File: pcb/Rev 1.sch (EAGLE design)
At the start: 218 parts, among them J1 3220-10-0100-00, J2 10118194-0001LF, J3 B2B-PH-K-S(LF)(SN), Q1 MMBT3904,215MMBT3904,215, Q12 MMBT3904,215MMBT3904,215, Q13 MMBT3904,215MMBT3904,215, Q14 MMBT3904,215MMBT3904,215, Q15 MMBT3904,215MMBT3904,215, Q16 TEFT4300, Q17 TEFT4300, Q18 TEFT4300, Q19 TEFT4300, Q20 MMBT3904,215MMBT3904,215, Q21 MMBT3904,215MMBT3904,215, Q22 MMBT3904,215MMBT3904,215, Q23 MMBT3904,215MMBT3904,215, Q24 TEFT4300, Q25 TEFT4300, Q26 TEFT4300, Q27 TEFT4300, Q28 SI7157DP, Q29 SI7157DP, Q30 MMBT3906, Q31 MMBT3906, Q32 SI7157DP, Q33 MMBT3906, Q34 MMBT3906, U1 ATSAMD21G18A-MU, U10 DRV8871, U11 PCAL6416A, U12 MAX7315, U2 AP3441, U3 TPS61089, U4 BNO055, U5 MCP73811, U7 DRV8871, U8 DRV8871, U9 DRV8871

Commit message: Placed and routed IO expanders
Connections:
- net IR2: now also U11.P1_5; no longer U11.P1_1
- net IR3: now also U11.P1_4; no longer U11.P1_2
- net IR5: now also U11.P1_1; no longer U11.P1_4
- net IR6: now also U11.P1_2; no longer U11.P1_5
- net LED2: now also U11.P0_3; no longer U11.P0_2
- net LED3: now also U11.P0_4; no longer U11.P0_3
- net LED4: now also U11.P0_2; no longer U11.P0_4
- net MOTOR_1A: now also U12.P3; no longer U12.P1
- net MOTOR_1B: now also U12.P4; no longer U12.P2
- net MOTOR_2A: now also U12.P1; no longer U12.P3
- net MOTOR_2B: now also U12.P2; no longer U12.P4
- net MOTOR_3A: now also U12.P7; no longer U12.P5
- net MOTOR_3B: now also U12.P8; no longer U12.P6
- net MOTOR_4A: now also U12.P5; no longer U12.P7
- net MOTOR_4B: now also U12.P6; no longer U12.P8
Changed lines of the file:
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@@
 </segment>
 <segment>
-<pinref part="U12" gate="G$1" pin="P1"/>
-<wire x1="246.38" y1="0" x2="264.16" y2="0" width="0.1524" layer="91"/>
-<label x="248.92" y="0" size="1.778" layer="95"/>
+<pinref part="U12" gate="G$1" pin="P3"/>
+<wire x1="246.38" y1="-5.08" x2="264.16" y2="-5.08" width="0.1524" layer="91"/>
+<label x="248.92" y="-5.08" size="1.778" layer="95"/>
 </segment>
 </net>
@@
 </segment>
 <segment>
-<pinref part="U12" gate="G$1" pin="P2"/>
-<wire x1="264.16" y1="-2.54" x2="246.38" y2="-2.54" width="0.1524" layer="91"/>
-<label x="248.92" y="-2.54" size="1.778" layer="95"/>
+<pinref part="U12" gate="G$1" pin="P4"/>
+<wire x1="264.16" y1="-7.62" x2="246.38" y2="-7.62" width="0.1524" layer="91"/>
+<label x="248.92" y="-7.62" size="1.778" layer="95"/>
 </segment>
 </net>
@@
 </segment>
 <segment>
-<pinref part="U12" gate="G$1" pin="P3"/>
-<wire x1="246.38" y1="-5.08" x2="264.16" y2="-5.08" width="0.1524" layer="91"/>
-<label x="248.92" y="-5.08" size="1.778" layer="95"/>
+<pinref part="U12" gate="G$1" pin="P1"/>
+<wire x1="246.38" y1="0" x2="264.16" y2="0" width="0.1524" layer="91"/>
+<label x="248.92" y="0" size="1.778" layer="95"/>
 </segment>
 </net>
@@
 </segment>
 <segment>
-<pinref part="U12" gate="G$1" pin="P4"/>
-<wire x1="264.16" y1="-7.62" x2="246.38" y2="-7.62" width="0.1524" layer="91"/>
-<label x="248.92" y="-7.62" size="1.778" layer="95"/>
+<pinref part="U12" gate="G$1" pin="P2"/>
+<wire x1="264.16" y1="-2.54" x2="246.38" y2="-2.54" width="0.1524" layer="91"/>
+<label x="248.92" y="-2.54" size="1.778" layer="95"/>
 </segment>
 </net>
@@
 </segment>
 <segment>
+<pinref part="U12" gate="G$1" pin="P7"/>
+<wire x1="264.16" y1="-15.24" x2="246.38" y2="-15.24" width="0.1524" layer="91"/>
+<label x="248.92" y="-15.24" size="1.778" layer="95"/>
+</segment>
+</net>
+<net name="MOTOR_3B" class="0">
+<segment>
+<pinref part="U9" gate="G$1" pin="IN2"/>
+<wire x1="0" y1="-55.88" x2="-15.24" y2="-55.88" width="0.1524" layer="91"/>
+<label x="-15.24" y="-55.88" size="1.778" layer="95"/>
+</segment>
+<segment>
+<pinref part="U12" gate="G$1" pin="P8"/>
+<wire x1="264.16" y1="-17.78" x2="246.38" y2="-17.78" width="0.1524" layer="91"/>
+<label x="248.92" y="-17.78" size="1.778" layer="95"/>
+</segment>
+</net>
+<net name="ENCODER_3A" class="0">
+<segment>
+<pinref part="A3" gate="G$1" pin="OUTA"/>
+<wire x1="58.42" y1="-50.8" x2="38.1" y2="-50.8" width="0.1524" layer="91"/>
+<label x="38.1" y="-50.8" size="1.778" layer="95"/>
+</segment>
+</net>
+<net name="ENCODER_3B" class="0">
+<segment>
+<pinref part="A3" gate="G$1" pin="OUTB"/>
+<wire x1="58.42" y1="-53.34" x2="38.1" y2="-53.34" width="0.1524" layer="91"/>
+<label x="38.1" y="-53.34" size="1.778" layer="95"/>
+</segment>
+</net>
+<net name="MOTOR_4A" class="0">
+<segment>
+<pinref part="U10" gate="G$1" pin="IN1"/>
+<wire x1="106.68" y1="-53.34" x2="91.44" y2="-53.34" width="0.1524" layer="91"/>
+<label x="91.44" y="-53.34" size="1.778" layer="95"/>
+</segment>
+<segment>
 <pinref part="U12" gate="G$1" pin="P5"/>
 <wire x1="264.16" y1="-10.16" x2="246.38" y2="-10.16" width="0.1524" layer="91"/>
@@
 </segment>
 </net>
-<net name="MOTOR_3B" class="0">
-<segment>
-<pinref part="U9" gate="G$1" pin="IN2"/>
-<wire x1="0" y1="-55.88" x2="-15.24" y2="-55.88" width="0.1524" layer="91"/>
-<label x="-15.24" y="-55.88" size="1.778" layer="95"/>
+<net name="MOTOR_4B" class="0">
+<segment>
+<pinref part="U10" gate="G$1" pin="IN2"/>
+<wire x1="106.68" y1="-55.88" x2="91.44" y2="-55.88" width="0.1524" layer="91"/>
+<label x="91.44" y="-55.88" size="1.778" layer="95"/>
 </segment>
 <segment>
@@
 <wire x1="264.16" y1="-12.7" x2="246.38" y2="-12.7" width="0.1524" layer="91"/>
 <label x="248.92" y="-12.7" size="1.778" layer="95"/>
-</segment>
-</net>
-<net name="ENCODER_3A" class="0">
-<segment>
-<pinref part="A3" gate="G$1" pin="OUTA"/>
-<wire x1="58.42" y1="-50.8" x2="38.1" y2="-50.8" width="0.1524" layer="91"/>
-<label x="38.1" y="-50.8" size="1.778" layer="95"/>
-</segment>
-</net>
-<net name="ENCODER_3B" class="0">
-<segment>
-<pinref part="A3" gate="G$1" pin="OUTB"/>
-<wire x1="58.42" y1="-53.34" x2="38.1" y2="-53.34" width="0.1524" layer="91"/>
-<label x="38.1" y="-53.34" size="1.778" layer="95"/>
-</segment>
-</net>
-<net name="MOTOR_4A" class="0">
-<segment>
-<pinref part="U10" gate="G$1" pin="IN1"/>
-<wire x1="106.68" y1="-53.34" x2="91.44" y2="-53.34" width="0.1524" layer="91"/>
-<label x="91.44" y="-53.34" size="1.778" layer="95"/>
-</segment>
-<segment>
-<pinref part="U12" gate="G$1" pin="P7"/>
-<wire x1="264.16" y1="-15.24" x2="246.38" y2="-15.24" width="0.1524" layer="91"/>
-<label x="248.92" y="-15.24" size="1.778" layer="95"/>
-</segment>
-</net>
-<net name="MOTOR_4B" class="0">
-<segment>
-<pinref part="U10" gate="G$1" pin="IN2"/>
-<wire x1="106.68" y1="-55.88" x2="91.44" y2="-55.88" width="0.1524" layer="91"/>
-<label x="91.44" y="-55.88" size="1.778" layer="95"/>
-</segment>
-<segment>
-<pinref part="U12" gate="G$1" pin="P8"/>
-<wire x1="264.16" y1="-17.78" x2="246.38" y2="-17.78" width="0.1524" layer="91"/>
-<label x="248.92" y="-17.78" size="1.778" layer="95"/>
 </segment>
 </net>
@@
 <net name="LED2" class="0">
 <segment>
-<pinref part="U11" gate="G$1" pin="P0_2"/>
-<wire x1="0" y1="-45.72" x2="10.16" y2="-45.72" width="0.1524" layer="91"/>
-<label x="0" y="-45.72" size="1.778" layer="95"/>
-</segment>
-<segment>
 <pinref part="R18" gate="G$1" pin="P$1"/>
 <wire x1="63.5" y1="5.08" x2="63.5" y2="2.54" width="0.1524" layer="91"/>
@@
 <label x="55.88" y="2.54" size="1.778" layer="95"/>
 </segment>
-</net>
-<net name="LED3" class="0">
 <segment>
 <pinref part="U11" gate="G$1" pin="P0_3"/>
@@
 <label x="0" y="-48.26" size="1.778" layer="95"/>
 </segment>
+</net>
+<net name="LED3" class="0">
 <segment>
 <pinref part="R19" gate="G$1" pin="P$1"/>
@@
 <label x="78.74" y="2.54" size="1.778" layer="95"/>
 </segment>
-</net>
-<net name="LED4" class="0">
 <segment>
 <pinref part="U11" gate="G$1" pin="P0_4"/>
@@
 <label x="0" y="-50.8" size="1.778" layer="95"/>
 </segment>
+</net>
+<net name="LED4" class="0">
 <segment>
 <pinref part="R20" gate="G$1" pin="P$1"/>
@@
 <label x="101.6" y="2.54" size="1.778" layer="95"/>
 </segment>
+<segment>
+<pinref part="U11" gate="G$1" pin="P0_2"/>
+<wire x1="0" y1="-45.72" x2="10.16" y2="-45.72" width="0.1524" layer="91"/>
+<label x="0" y="-45.72" size="1.778" layer="95"/>
+</segment>
 </net>
 <net name="N$25" class="0">
@@
 </segment>
 </net>
-<net name="IR2" class="0">
+<net name="IR3" class="0">
+<segment>
+<pinref part="U11" gate="G$1" pin="P1_4"/>
+<wire x1="48.26" y1="-50.8" x2="40.64" y2="-50.8" width="0.1524" layer="91"/>
+<label x="43.18" y="-50.8" size="1.778" layer="95"/>
+</segment>
+</net>
+<net name="IR4" class="0">
+<segment>
+<pinref part="U11" gate="G$1" pin="P1_3"/>
+<wire x1="48.26" y1="-48.26" x2="40.64" y2="-48.26" width="0.1524" layer="91"/>
+<label x="43.18" y="-48.26" size="1.778" layer="95"/>
+</segment>
+</net>
+<net name="IR7" class="0">
+<segment>
+<pinref part="U11" gate="G$1" pin="P1_6"/>
+<wire x1="48.26" y1="-55.88" x2="40.64" y2="-55.88" width="0.1524" layer="91"/>
+<label x="43.18" y="-55.88" size="1.778" layer="95"/>
+</segment>
+</net>
+<net name="IR8" class="0">
+<segment>
+<pinref part="U11" gate="G$1" pin="P1_7"/>
+<wire x1="48.26" y1="-58.42" x2="40.64" y2="-58.42" width="0.1524" layer="91"/>
+<label x="43.18" y="-58.42" size="1.778" layer="95"/>
+</segment>
+</net>
+<net name="IR5" class="0">
 <segment>
 <pinref part="U11" gate="G$1" pin="P1_1"/>
@@
 </segment>
 </net>
-<net name="IR3" class="0">
+<net name="IR6" class="0">
 <segment>
 <pinref part="U11" gate="G$1" pin="P1_2"/>
@@
 </segment>
 </net>
-<net name="IR4" class="0">
-<segment>
-<pinref part="U11" gate="G$1" pin="P1_3"/>
-<wire x1="48.26" y1="-48.26" x2="40.64" y2="-48.26" width="0.1524" layer="91"/>
-<label x="43.18" y="-48.26" size="1.778" layer="95"/>
-</segment>
-</net>
-<net name="IR5" class="0">
-<segment>
-<pinref part="U11" gate="G$1" pin="P1_4"/>
-<wire x1="48.26" y1="-50.8" x2="40.64" y2="-50.8" width="0.1524" layer="91"/>
-<label x="43.18" y="-50.8" size="1.778" layer="95"/>
-</segment>
-</net>
-<net name="IR6" class="0">
+<net name="IR2" class="0">
 <segment>
 <pinref part="U11" gate="G$1" pin="P1_5"/>
@@
 </segment>
 </net>
-<net name="IR7" class="0">
-<segment>
-<pinref part="U11" gate="G$1" pin="P1_6"/>
-<wire x1="48.26" y1="-55.88" x2="40.64" y2="-55.88" width="0.1524" layer="91"/>
-<label x="43.18" y="-55.88" size="1.778" layer="95"/>
-</segment>
-</net>
-<net name="IR8" class="0">
-<segment>
-<pinref part="U11" gate="G$1" pin="P1_7"/>
-<wire x1="48.26" y1="-58.42" x2="40.64" y2="-58.42" width="0.1524" layer="91"/>
-<label x="43.18" y="-58.42" size="1.778" layer="95"/>
-</segment>
-</net>

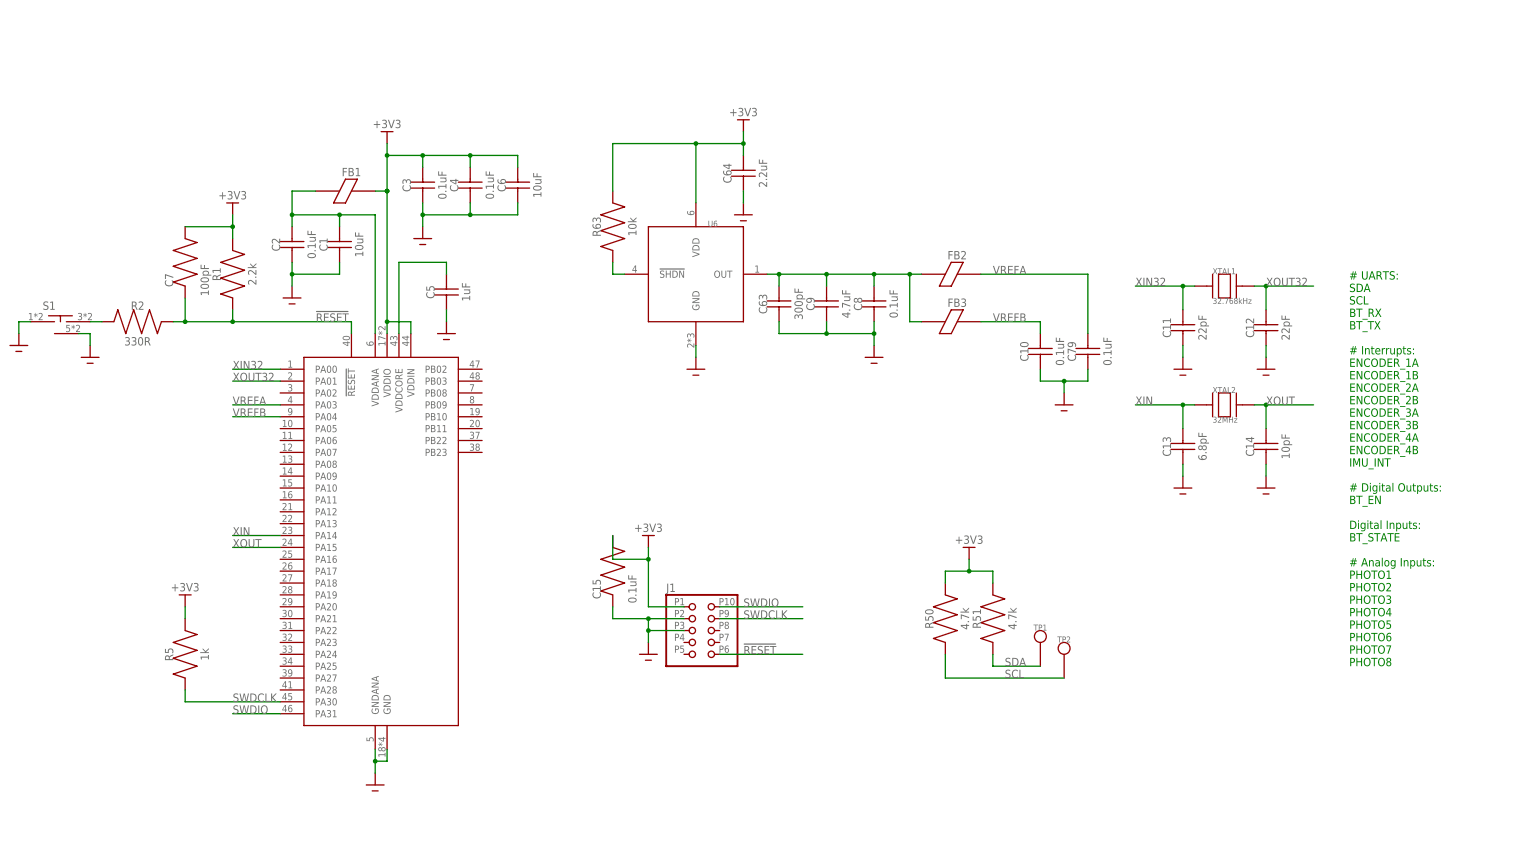
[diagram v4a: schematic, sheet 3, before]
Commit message: Finished routing signals to MCU
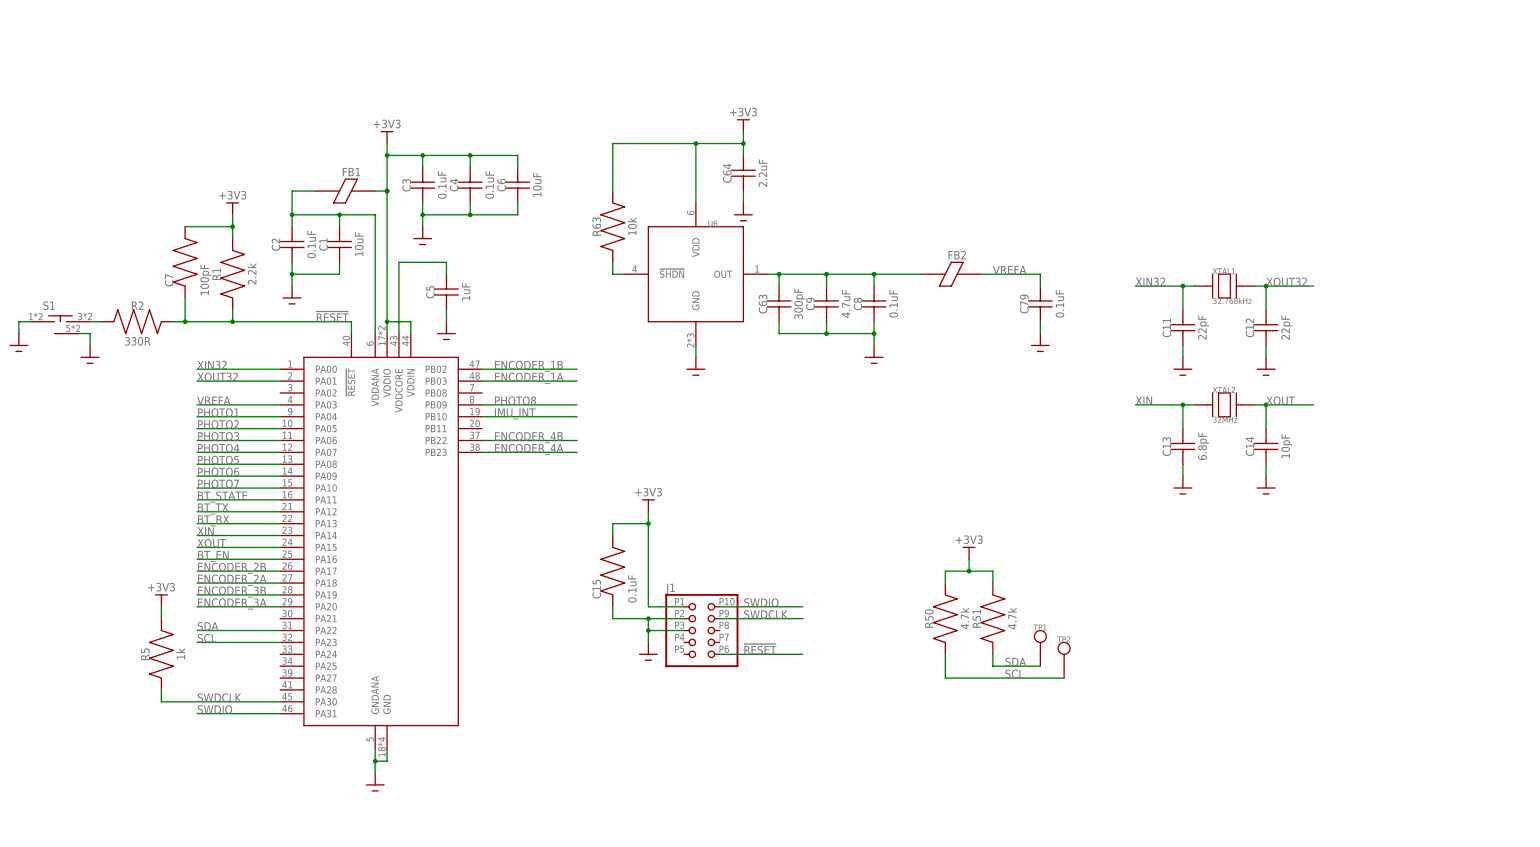
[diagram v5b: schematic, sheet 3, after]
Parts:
- removed C10: 0.1uF, Micromouse 2020:CAPACITOR0402
- removed FB3: (no value), Micromouse 2020:FERRITE0402
- C78: device Micromouse 2020:CAPACITOR0805 -> Micromouse 2020:CAPACITOR0603
- R2: device Micromouse 2020:RESISTOR0603 -> Micromouse 2020:RESISTOR0805
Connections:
- removed net VREFB: C10.P$2, FB3.P$2, U1.PA04
- net BT_EN: now also U1.PA16
- net BT_RX: now also U1.PA13
- net BT_STATE: now also U1.PA11
- net BT_TX: now also U1.PA12
- net ENCODER_1A: now also U1.PB03
- net ENCODER_1B: now also U1.PB02
- net ENCODER_2A: now also U1.PA18
- net ENCODER_2B: now also U1.PA17
- net ENCODER_3A: now also U1.PA20
- net ENCODER_3B: now also U1.PA19
- net ENCODER_4A: now also U1.PB23
- net ENCODER_4B: now also U1.PB22
- net GND: no longer C10.P$1
- net IMU_INT: now also U1.PB10
- net N$999: no longer FB3.P$1
- net PHOTO1: now also U1.PA04
- net PHOTO2: now also U1.PA05
- net PHOTO3: now also U1.PA06
- net PHOTO4: now also U1.PA07
- net PHOTO5: now also U1.PA08
- net PHOTO6: now also U1.PA09
- net PHOTO7: now also U1.PA10
- net PHOTO8: now also U1.PB09
- net SCL: now also U1.PA23
- net SDA: now also U1.PA22
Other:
- note removed: "# UARTS: SDA SCL BT_RX BT_TX # Interrupts: ENCODER_1A ENCODER_1B ENCODER_2A ENCODER_2B ENCODER_3A ENCODER_3B ENCODER_4A ENCODER_4B IMU_INT # Digital Outputs: BT_EN Digital Inputs: BT_STATE # Analog Inputs: PHOTO1 PHOTO2 PHOTO3 PHOTO4 PHOTO5 PHOTO6 PHOTO7 PHOTO8"
- moved on the sheet: C79, R5

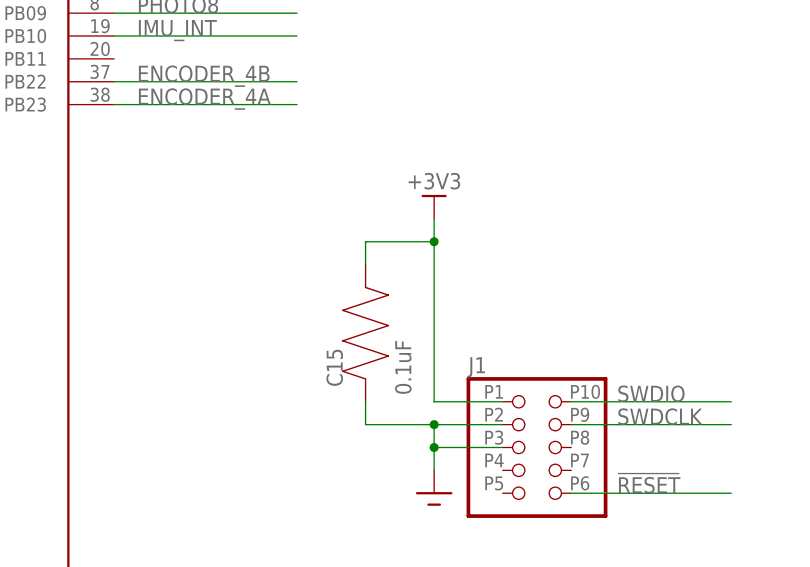
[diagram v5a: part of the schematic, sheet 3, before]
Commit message: Fixed passive type
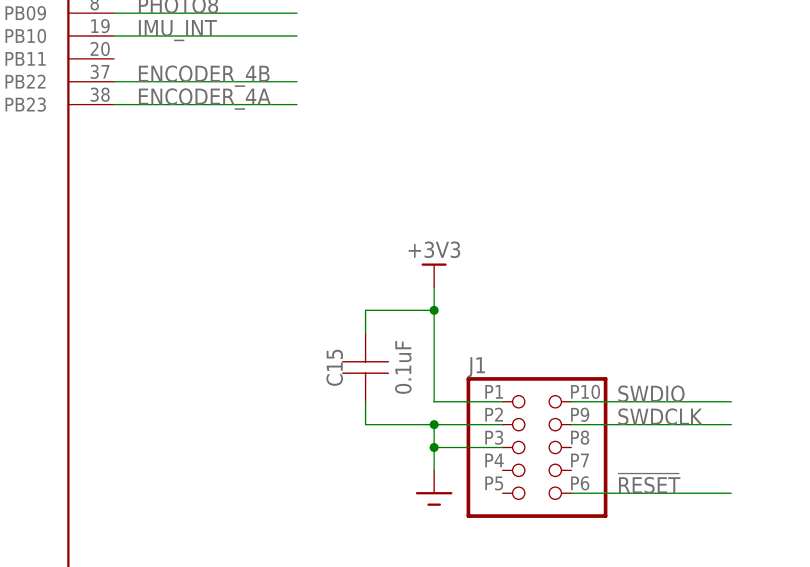
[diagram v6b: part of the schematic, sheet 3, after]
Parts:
- C15: device Micromouse 2020:RESISTOR0603 -> Micromouse 2020:CAPACITOR0603
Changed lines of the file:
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@@
 <part name="P+4" library="Micromouse 2020" deviceset="+3V3" device=""/>
 <part name="P+5" library="Micromouse 2020" deviceset="+3V3" device=""/>
-<part name="C15" library="Micromouse 2020" deviceset="RESISTOR" device="0603" package3d_urn="urn:adsk.eagle:package:16053670/1" value="0.1uF"/>
+<part name="C15" library="Micromouse 2020" deviceset="CAPACITOR" device="0603" package3d_urn="urn:adsk.eagle:package:16053670/1" value="0.1uF"/>
 <part name="GND13" library="Micromouse 2020" deviceset="GND" device=""/>
 <part name="U2" library="Micromouse 2020" deviceset="AP3441" device="" package3d_urn="urn:adsk.eagle:package:14523753/1"/>
@@
 <attribute name="VALUE" x="-48.26" y="-7.62" size="1.778" layer="96" rot="R180" align="bottom-center"/>
 </instance>
-<instance part="P+5" gate="G$1" x="55.88" y="10.16" smashed="yes">
-<attribute name="VALUE" x="55.88" y="12.7" size="1.778" layer="96" rot="R180" align="bottom-center"/>
+<instance part="P+5" gate="G$1" x="55.88" y="2.54" smashed="yes">
+<attribute name="VALUE" x="55.88" y="5.08" size="1.778" layer="96" rot="R180" align="bottom-center"/>
 </instance>
 <instance part="C15" gate="G$1" x="48.26" y="-12.7" smashed="yes" rot="R90">
@@
 <pinref part="P+5" gate="G$1" pin="+3V3"/>
 <wire x1="63.5" y1="-12.7" x2="55.88" y2="-12.7" width="0.1524" layer="91"/>
-<wire x1="55.88" y1="-12.7" x2="55.88" y2="5.08" width="0.1524" layer="91"/>
+<wire x1="55.88" y1="-12.7" x2="55.88" y2="-2.54" width="0.1524" layer="91"/>
 <pinref part="C15" gate="G$1" pin="P$2"/>
-<wire x1="55.88" y1="5.08" x2="55.88" y2="7.62" width="0.1524" layer="91"/>
-<wire x1="48.26" y1="2.54" x2="48.26" y2="5.08" width="0.1524" layer="91"/>
-<wire x1="48.26" y1="5.08" x2="55.88" y2="5.08" width="0.1524" layer="91"/>
-<junction x="55.88" y="5.08"/>
-</segment>
-<segment>
+<wire x1="55.88" y1="-2.54" x2="55.88" y2="0" width="0.1524" layer="91"/>
+<wire x1="48.26" y1="-5.08" x2="48.26" y2="-2.54" width="0.1524" layer="91"/>
+<wire x1="48.26" y1="-2.54" x2="55.88" y2="-2.54" width="0.1524" layer="91"/>
+<junction x="55.88" y="-2.54"/>
+</segment>
+<segment>
